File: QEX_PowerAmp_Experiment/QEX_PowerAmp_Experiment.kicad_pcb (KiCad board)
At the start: 2 copper layers, 87 x 75.5 mm, 73 parts, among them J1 Key In, J10 Conn_01x02, J11 SMA, J12 Conn_01x02, J2 Key In, J3 Conn_01x02, J4 Conn_01x02, J5 SMA, J6 Conn_01x02, J7 Conn_01x02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

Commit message: Starting layout work
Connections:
- net Net-(C12-Pad1) renamed /k4
- net Net-(C4-Pad1) renamed /k1
- net Net-(D1-K) renamed /base
- net Net-(J1-In) renamed /keyIn
- net Net-(J10-Pin_1) renamed /th_out
- net Net-(J12-Pin_2) renamed /VDD_PWR
- net Net-(J4-Pin_1) renamed /cs_out
- net Net-(J9-Pin_1) renamed /k8
- net Net-(J9-Pin_2) renamed /k9
- net Net-(Q2A-D) renamed /D2
- net Net-(Q2A-G) renamed /G2
- net Net-(Q2B-D) renamed /D1
- net Net-(Q2B-G) renamed /G1
- net Net-(Q3A-B1) renamed /cm1
- net Net-(Q3B-C2) renamed /cm2
- net Net-(U7-FB) renamed /fb
- net Net-(U7-SW) renamed /sw
- net Net-(U8A-+) renamed /k2
- net Net-(U8A--) renamed /k3
- net Net-(U8B-+) renamed /k5
- net Net-(U8B--) renamed /k6
- net Net-(U8C--) renamed /k7
- net Net-(U8D-+) renamed /th1
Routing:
- added copper zone on F.Cu, net /VDD_AMP
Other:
- copper layers 2 -> 4

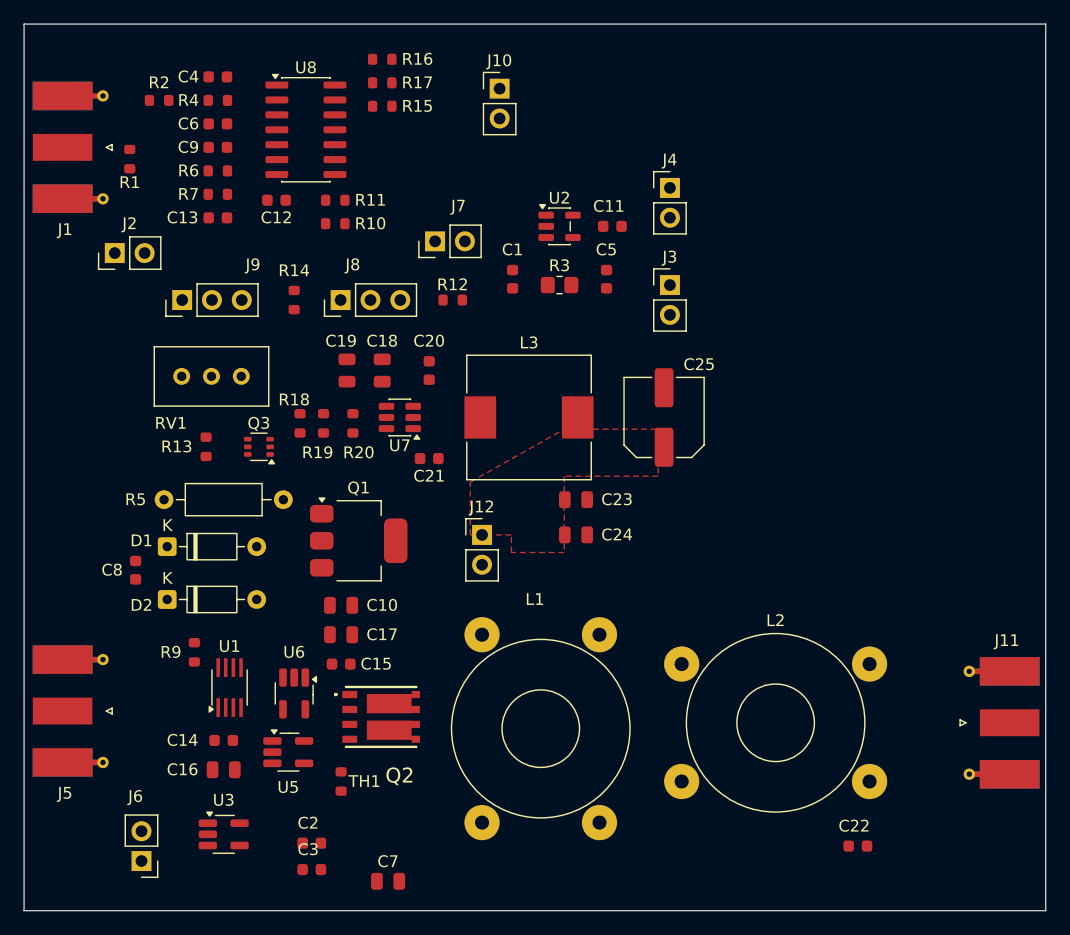
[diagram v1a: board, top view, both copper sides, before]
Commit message: Starting layout connections
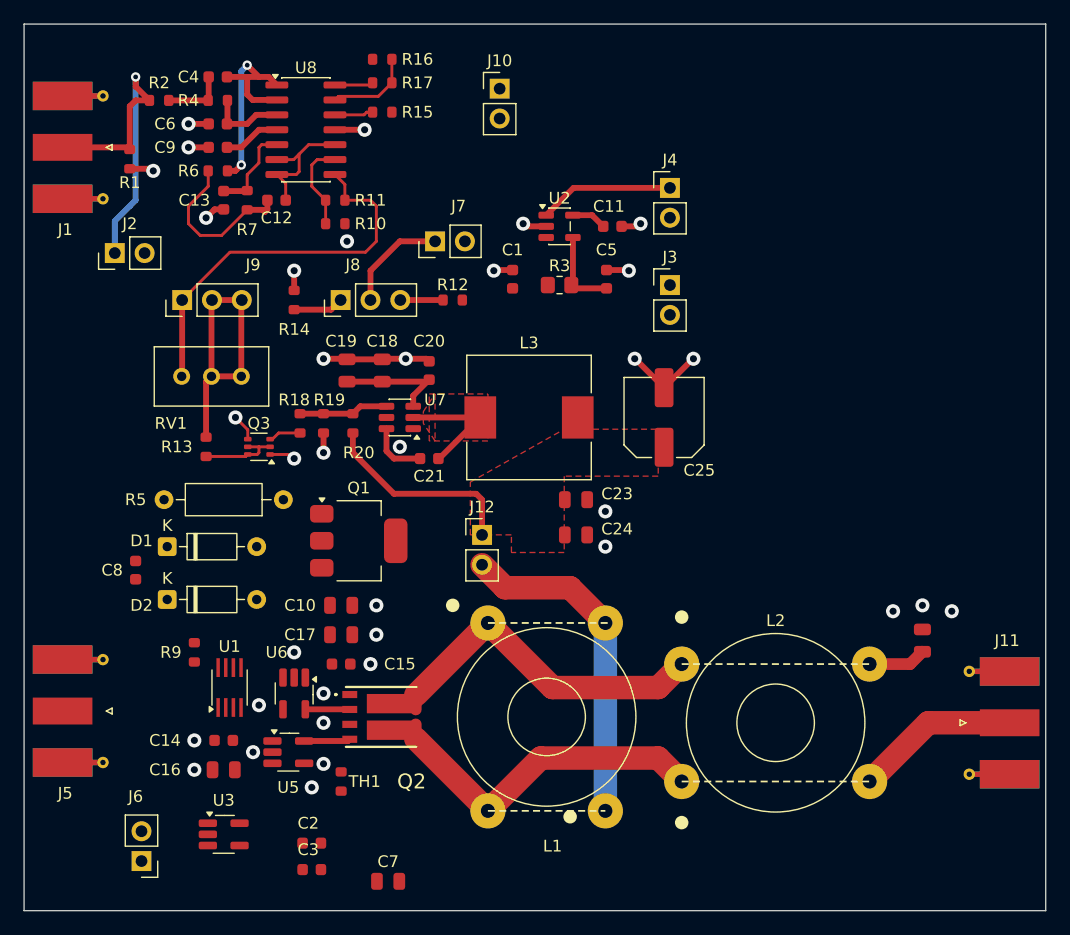
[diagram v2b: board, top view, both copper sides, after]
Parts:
- removed C22: 100nF, PCM_JLCPCB:C_0603
- added C26: 100nF, PCM_JLCPCB:C_0805, F.Cu at (179.0, 105.5)
- moved L1 19.5 mm to (142.0, 104.0), turned to -90 degrees
- moved R7 2.55 mm to (121.5, 68.0), turned to 90 degrees
- moved C13 1.58 mm to (119.5, 68.0), turned to -90 degrees
- moved R15 0.50 mm to (133.0, 60.5)
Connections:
- C1 pad 1: +12V -> Net-(J3-Pin_1)
- C9 pad 1: +12V -> +12VA
- J3 pad 1: +12V -> Net-(J3-Pin_1)
- L1 pad 1: /VDD_PWR -> /D2
- L1 pad 2: /D2 -> /D1
- L1 pad 3: /D1 -> /VDD_PWR
- Q1 pad 2: +12V -> +12VA
- Q1 pad 4: +12V -> +12VA
- R3 pad 1: +12V -> Net-(J3-Pin_1)
- R5 pad 1: +12V -> +12VA
- U2 pad 3: +12V -> Net-(J3-Pin_1)
- U8 pad 4: +12V -> +12VA
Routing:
- net GND: track 0.00 -> 41.2 mm, vias 0 -> 36
- net /k8: track 0.00 -> 33.6 mm
- net /D2: track 0.00 -> 30.1 mm
- net /D1: track 0.00 -> 29.7 mm
- net /keyIn: track 0.00 -> 29.6 mm, vias 0 -> 1
- net /VDD_PWR: track 0.00 -> 28.6 mm
- net /k9: track 0.00 -> 23.5 mm
- net +12VA: track 0.00 -> 22.0 mm
- net /k3: track 0.00 -> 20.3 mm, vias 0 -> 2
- net /VDD_AMP: track 0.00 -> 17.3 mm
- net /k4: track 0.00 -> 14.2 mm
- net /rf_out: track 0.00 -> 14.0 mm
- net /cs_out: track 0.00 -> 11.5 mm
- net /k6: track 0.00 -> 11.5 mm
- net /sw: track 0.00 -> 10.7 mm
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- added copper zone on F.Cu, net /sw

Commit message: First pass of completed routing
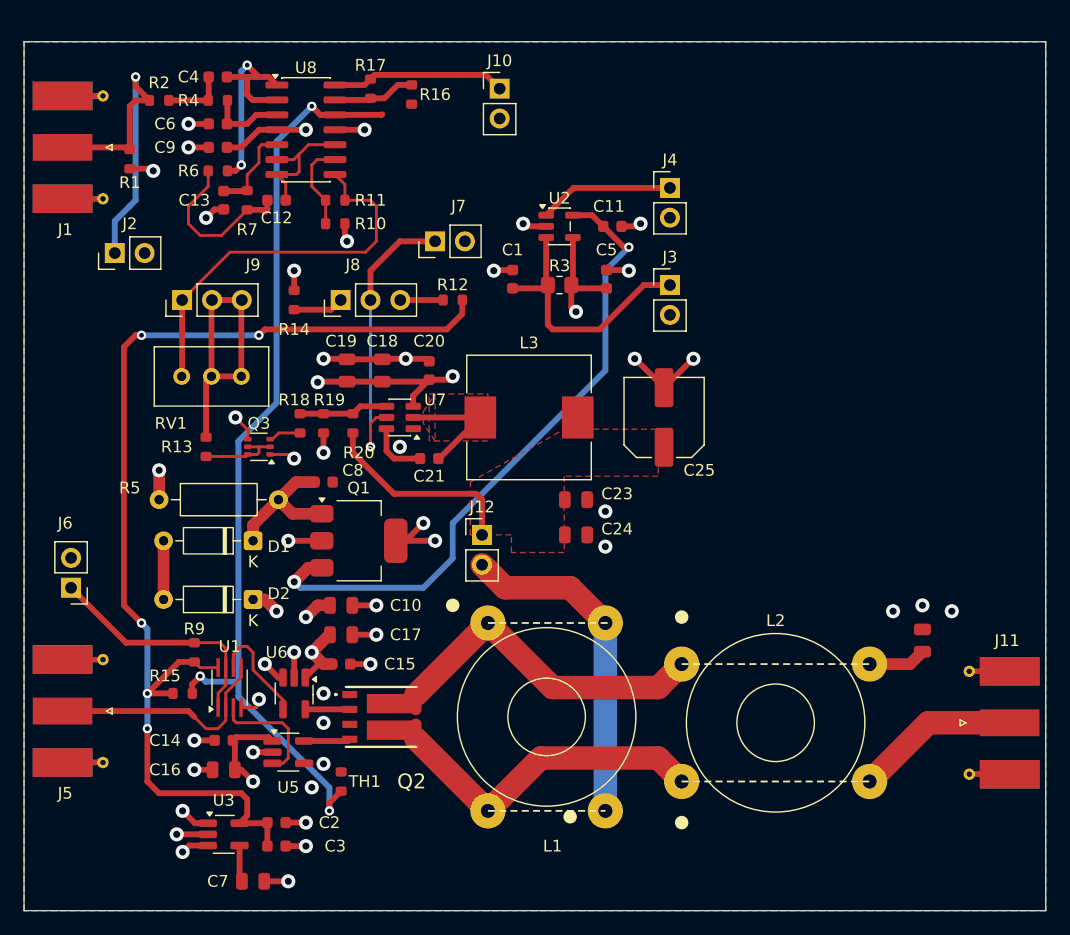
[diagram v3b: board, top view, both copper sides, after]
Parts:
- moved R15 52.3 mm to (116.0, 110.0), turned to 0 degrees
- moved J6 24.0 mm to (106.5, 101.0)
- moved C8 17.7 mm to (128.0, 92.0), turned to 0 degrees
- moved C7 11.5 mm to (122.0, 126.0)
- moved R5 10.6 mm to (114.0, 93.5), turned to 0 degrees
- moved D1 7.33 mm to (122.0, 97.0), turned to 180 degrees
- moved D2 7.31 mm to (122.0, 102.0), turned to 180 degrees
- moved R16 3.91 mm to (135.5, 59.0), turned to -90 degrees
- moved C3 3.61 mm to (124.0, 123.0)
- moved C2 3.47 mm to (124.0, 121.0)
- moved R17 1.12 mm to (132.0, 58.5), turned to 90 degrees
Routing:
- net +3.3V: track 0.00 -> 94.3 mm, vias 0 -> 5
- net +5VA: track 2.98 -> 80.1 mm, vias 0 -> 8
- net /th1: track 3.30 -> 79.4 mm, vias 0 -> 3
- net GND: track 41.2 -> 68.2 mm, vias 36 -> 41
- net Net-(J3-Pin_1): track 0.00 -> 22.7 mm
- net +12VA: track 22.0 -> 43.2 mm, vias 0 -> 8
- net /~{rf_enable}: track 0.00 -> 20.6 mm
- net /rfin: track 0.00 -> 19.9 mm
- net /sw_enable: track 9.04 -> 25.1 mm, vias 0 -> 1
- net /base: track 0.00 -> 12.3 mm
- net /th_out: track 3.28 -> 14.9 mm
- net /rfd+: track 0.00 -> 10.1 mm
- net /rfd-: track 0.00 -> 9.19 mm
- net Net-(D1-A): track 0.00 -> 5.00 mm
- net Net-(U3-BP): track 0.00 -> 3.13 mm
- added copper zone on In2.Cu, net +12VA
- added copper zone on In2.Cu, net +5VA
- added copper zone on B.Cu, net GND
- added copper zone on F.Cu, net GND
- added copper zone on In1.Cu, net GND
- added copper zone on In2.Cu, net GND
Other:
- board size 87 x 75.5 mm -> 87 x 74 mm

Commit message: Layout refinement
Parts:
- moved J3 28.0 mm to (185.5, 75.2)
- moved J7 24.2 mm to (158.2, 59.0)
- moved J4 15.9 mm to (171.2, 59.0), turned to 90 degrees
- moved J6 4.72 mm to (106.5, 96.3)
- moved J2 4.62 mm to (106.5, 75.2), turned to 0 degrees
- moved C20 1.00 mm to (137.0, 83.5), turned to 0 degrees
- turned C18 to -90 degrees
- turned C19 to -90 degrees
- turned J10 to 90 degrees
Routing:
- net /sw_enable: track 25.1 -> 60.8 mm
- net Net-(J3-Pin_1): track 22.7 -> 50.7 mm
- net +5VA: track 80.1 -> 103.6 mm
- net /cs_out: track 11.5 -> 31.6 mm
- net /th1: track 79.4 -> 89.5 mm
- net /keyIn: track 29.6 -> 34.4 mm
- net /~{rf_enable}: track 20.6 -> 25.3 mm
- net +12VA: track 43.2 -> 41.3 mm
- net GND: track 68.2 -> 67.8 mm, vias 41 -> 111
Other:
- board text added: "Current Sense Output"
- board text added: "Ext. Gain Control"
- board text added: "Gain Control"
- board text added: "Keyer Input"
- board text added: "QRP Amplifier Test Board Version 1.0 N7WMN"
- board text added: "RF Clock Input"
- board text added: "RF Enable"
- board text added: "RF Output"
- board text added: "Supply Input 13.8V nominal"
- board text added: "Switch Enable"
- board text added: "Thermistor Output"
- board text added: "gnd"
- board text added: "jumper"

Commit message: Clean DRC
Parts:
- moved R9 0.50 mm to (117.0, 106.0)
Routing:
- net /th1: track 89.5 -> 85.5 mm
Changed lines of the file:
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@@
 	(footprint "PCM_JLCPCB:R_0603"
 		(layer "F.Cu")
-		(at 117 106.5 90)
+		(at 117 106 90)
 		(descr "Resistor SMD 0603 (1608 Metric), square (rectangular) end terminal, IPC_7351 nominal, (Body size source: IPC-SM-782 page 72, https://www.pcb-3d.com/wordpress/wp-content/uploads/ipc-sm-782a_amendment_1_and_2.pdf), generated with kicad-footprint-generator")
 		(tags "resistor")
@@
 				(font
 					(size 1.27 1.27)
-					(thickness 0.254)
+					(thickness 0.15875)
 				)
 			)
@@
 		(effects
 			(font
-				(size 0.75 0.75)
+				(size 0.8 0.8)
 				(thickness 0.125)
 			)
@@
 		(effects
 			(font
-				(size 0.75 0.75)
+				(size 0.8 0.8)
 				(thickness 0.125)
 			)
@@
 		(effects
 			(font
-				(size 0.75 0.75)
+				(size 0.8 0.8)
 				(thickness 0.125)
 			)
@@
 		(effects
 			(font
-				(size 0.75 0.75)
+				(size 0.8 0.8)
 				(thickness 0.125)
 			)
@@
 		(effects
 			(font
-				(size 0.75 0.75)
+				(size 0.8 0.8)
 				(thickness 0.125)
 			)
@@
 		(effects
 			(font
-				(size 0.75 0.75)
+				(size 0.8 0.8)
 				(thickness 0.125)
 			)
@@
 	)
 	(via
-		(at 137.5 100)
+		(at 137.5 99.5)
 		(size 1.2)
 		(drill 0.6)
@@
 	)
 	(via
-		(at 134.5 89)
+		(at 134.5 88.5)
 		(size 1.2)
 		(drill 0.6)
@@
 	)
 	(segment
-		(start 115.68 107.32)
-		(end 117 107.32)
-		(width 0.5)
-		(layer "F.Cu")
-		(net 2)
-	)
-	(segment
-		(start 117.48 107.8)
-		(end 117 107.32)
-		(width 0.25)
-		(layer "F.Cu")
-		(net 2)
-	)
-	(segment
 		(start 113 117.5)
 		(end 113 113)
@@
 	)
 	(segment
+		(start 119.025 107.8)
+		(end 118.545 107.32)
+		(width 0.25)
+		(layer "F.Cu")
+		(net 2)
+	)
+	(segment
 		(start 114 118.5)
 		(end 113 117.5)
@@
 	)
 	(segment
+		(start 118.545 107.32)
+		(end 117.5 107.32)
+		(width 0.25)
+		(layer "F.Cu")
+		(net 2)
+	)
+	(segment
 		(start 115.18 110)
 		(end 113 110)
@@
 	)
 	(segment
-		(start 119.025 107.8)
-		(end 117.48 107.8)
+		(start 112.5 79.5)
+		(end 112 79.5)
+		(width 0.5)
+		(layer "F.Cu")
+		(net 2)
+	)
+	(segment
+		(start 117.5 107.32)
+		(end 117 106.82)
 		(width 0.25)
 		(layer "F.Cu")
@@
 	)
 	(segment
-		(start 112.5 79.5)
-		(end 112 79.5)
+		(start 115.68 107.32)
+		(end 116.5 107.32)
 		(width 0.5)
 		(layer "F.Cu")
@@
 		(net 2)
 	)
+	(segment
+		(start 116.5 107.32)
+		(end 117 106.82)
+		(width 0.5)
+		(layer "F.Cu")
+		(net 2)
+	)
 	(via
 		(at 113 110)
-		(size 0.8)
+		(size 1)
 		(drill 0.4)
 		(layers "F.Cu" "B.Cu")
@@
 	(via
 		(at 122.5 79.5)
-		(size 0.8)
+		(size 1)
 		(drill 0.4)
 		(layers "F.Cu" "B.Cu")
@@
 	(via
 		(at 112.5 104)
-		(size 0.8)
+		(size 1)
 		(drill 0.4)
 		(layers "F.Cu" "B.Cu")
@@
 	(via
 		(at 112.5 79.5)
-		(size 0.8)
+		(size 1)
 		(drill 0.4)
 		(layers "F.Cu" "B.Cu")
@@
 	(via
 		(at 113 113)
-		(size 0.8)
+		(size 1)
 		(drill 0.4)
 		(layers "F.Cu" "B.Cu")
@@
 	(via
 		(at 154 72)
-		(size 0.8)
+		(size 1)
 		(drill 0.4)
 		(layers "F.Cu" "B.Cu")
@@
 	)
 	(segment
-		(start 106.5 101)
-		(end 106.5 96.275)
+		(start 111.18 105.68)
+		(end 116.5 105.68)
+		(width 0.5)
+		(layer "F.Cu")
+		(net 10)
+	)
+	(segment
+		(start 116.5 105.68)
+		(end 117 105.18)
 		(width 0.5)
 		(layer "F.Cu")
@@
 	)
 	(segment
-		(start 111.18 105.68)
-		(end 117 105.68)
+		(start 106.5 101)
+		(end 111.18 105.68)
 		(width 0.5)
 		(layer "F.Cu")
@@
 	)
 	(segment
-		(start 106.5 101)
-		(end 111.18 105.68)
-		(width 0.5)
+		(start 117 105.18)
+		(end 117.5 105.68)
+		(width 0.25)
 		(layer "F.Cu")
 		(net 10)
@@
 	)
 	(segment
-		(start 117 105.68)
-		(end 119.18 105.68)
+		(start 119.18 105.68)
+		(end 119.675 106.175)
 		(width 0.25)
 		(layer "F.Cu")
@@
 	)
 	(segment
-		(start 119.675 106.175)
-		(end 119.675 107.8)
+		(start 106.5 96.275)
+		(end 106.5 101)
+		(width 0.5)
+		(layer "F.Cu")
+		(net 10)
+	)
+	(segment
+		(start 117.5 105.68)
+		(end 119.18 105.68)
 		(width 0.25)
 		(layer "F.Cu")
@@
 	)
 	(segment
-		(start 119.18 105.68)
-		(end 119.675 106.175)
+		(start 119.675 106.175)
+		(end 119.675 107.8)
 		(width 0.25)
 		(layer "F.Cu")
@@
 	(via
 		(at 132 89)
-		(size 0.8)
+		(size 1)
 		(drill 0.4)
 		(layers "F.Cu" "B.Cu")
@@
 	(via
 		(at 121 65)
-		(size 0.8)
+		(size 1)
 		(drill 0.4)
 		(layers "F.Cu" "B.Cu")
@@
 	(via
 		(at 121.5 56.5)
-		(size 0.8)
+		(size 1)
 		(drill 0.4)
 		(layers "F.Cu" "B.Cu")
@@
 	(via
 		(at 112 57.5)
-		(size 0.8)
+		(size 1)
 		(drill 0.4)
 		(layers "F.Cu" "B.Cu")
@@
 	)
 	(segment
-		(start 132.95 60.73)
-		(end 133 60.68)
-		(width 0.5)
-		(layer "F.Cu")
-		(net 38)
-	)
-	(segment
-		(start 128.975 60.73)
-		(end 132.95 60.73)
-		(width 0.5)
-		(layer "F.Cu")
-		(net 38)
-	)
-	(segment
 		(start 127.73 60.73)
 		(end 127 60)
@@
 	(via
 		(at 117.5 108.525)
-		(size 0.8)
+		(size 1)
 		(drill 0.4)
 		(layers "F.Cu" "B.Cu")
@@
 	(via
 		(at 127 60)
-		(size 0.8)
+		(size 1)
 		(drill 0.4)
 		(layers "F.Cu" "B.Cu")
@@
 	(via
 		(at 128.5 120)
-		(size 0.8)
+		(size 1)
 		(drill 0.4)
 		(layers "F.Cu" "B.Cu")
@@
 	)
 	(segment
+		(start 146.9625 75.0875)
+		(end 146.9625 71.226)
+		(width 0.5)
+		(layer "F.Cu")
+		(net 41)
+	)
+	(segment
 		(start 155.275 75.225)
 		(end 185.5 75.225)
@@
 		(width 1)
 		(layer "F.Cu")
-		(net 41)
-	)
-	(segment
-		(start 146.9625 71.175)
-		(end 146.9625 75.0875)
-		(width 1)
-		(layer "F.Cu")
